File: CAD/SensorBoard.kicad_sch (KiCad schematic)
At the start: 37 parts, among them J1 USB C 2.0, SW1 BOOT_SW, U1 USBLC6-2SC6, U2 MIC5365-3.3YD5, U3 BME680, U4 TC1047xNB, U5 BMI323, X1 32MHz, X2 32kHz768

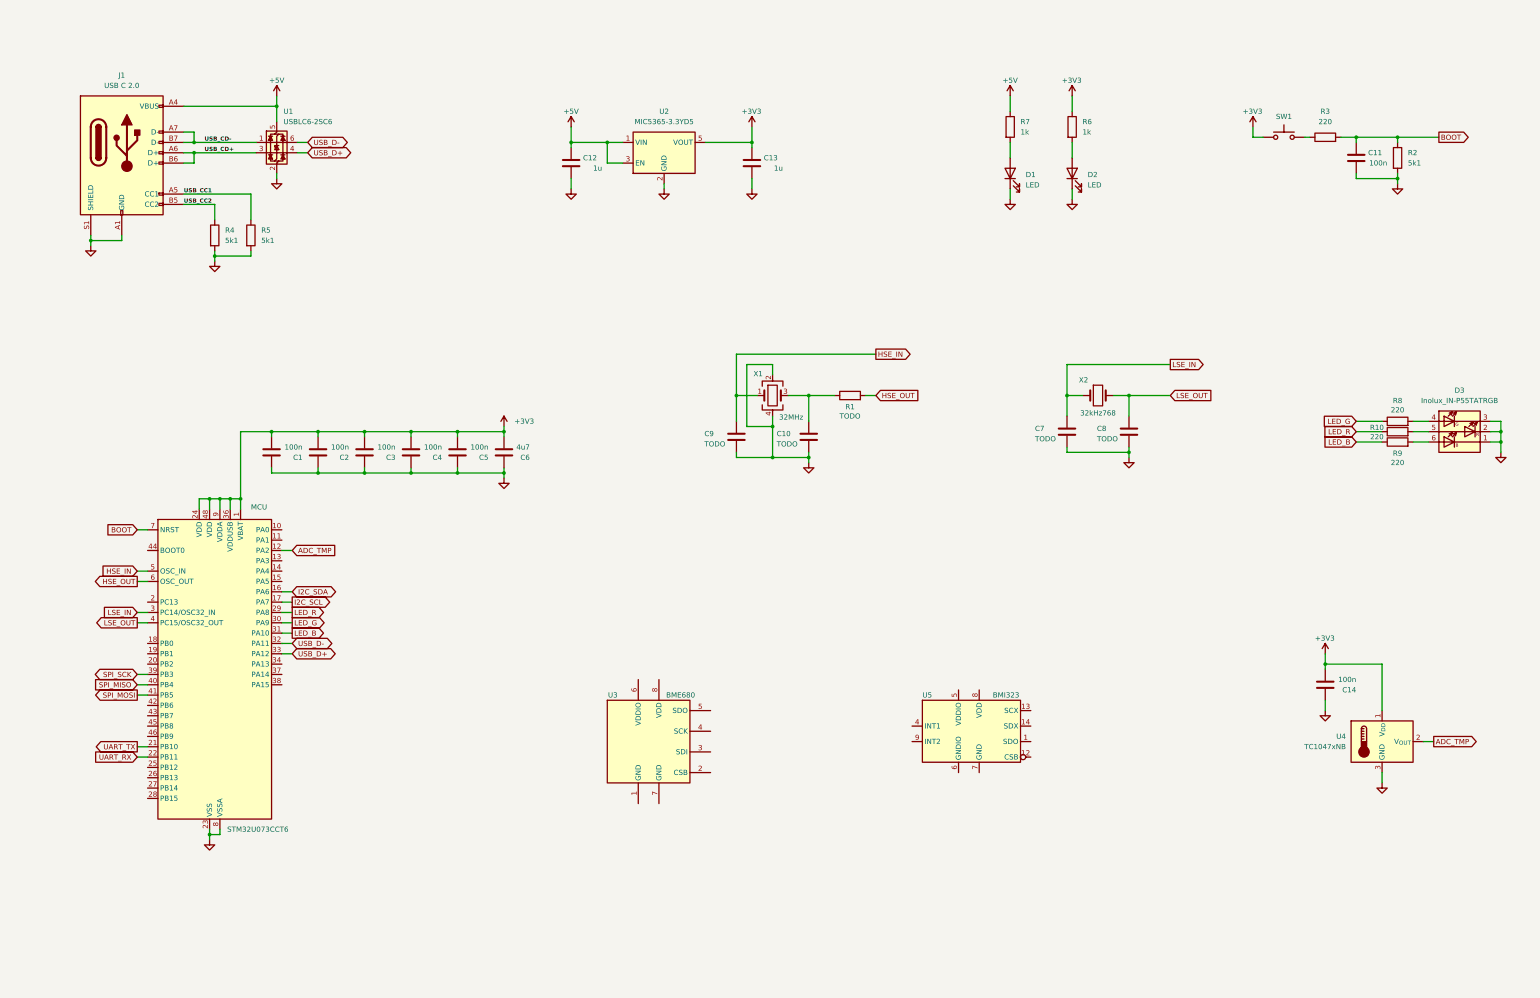
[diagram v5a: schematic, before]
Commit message: Update BME630 footprint
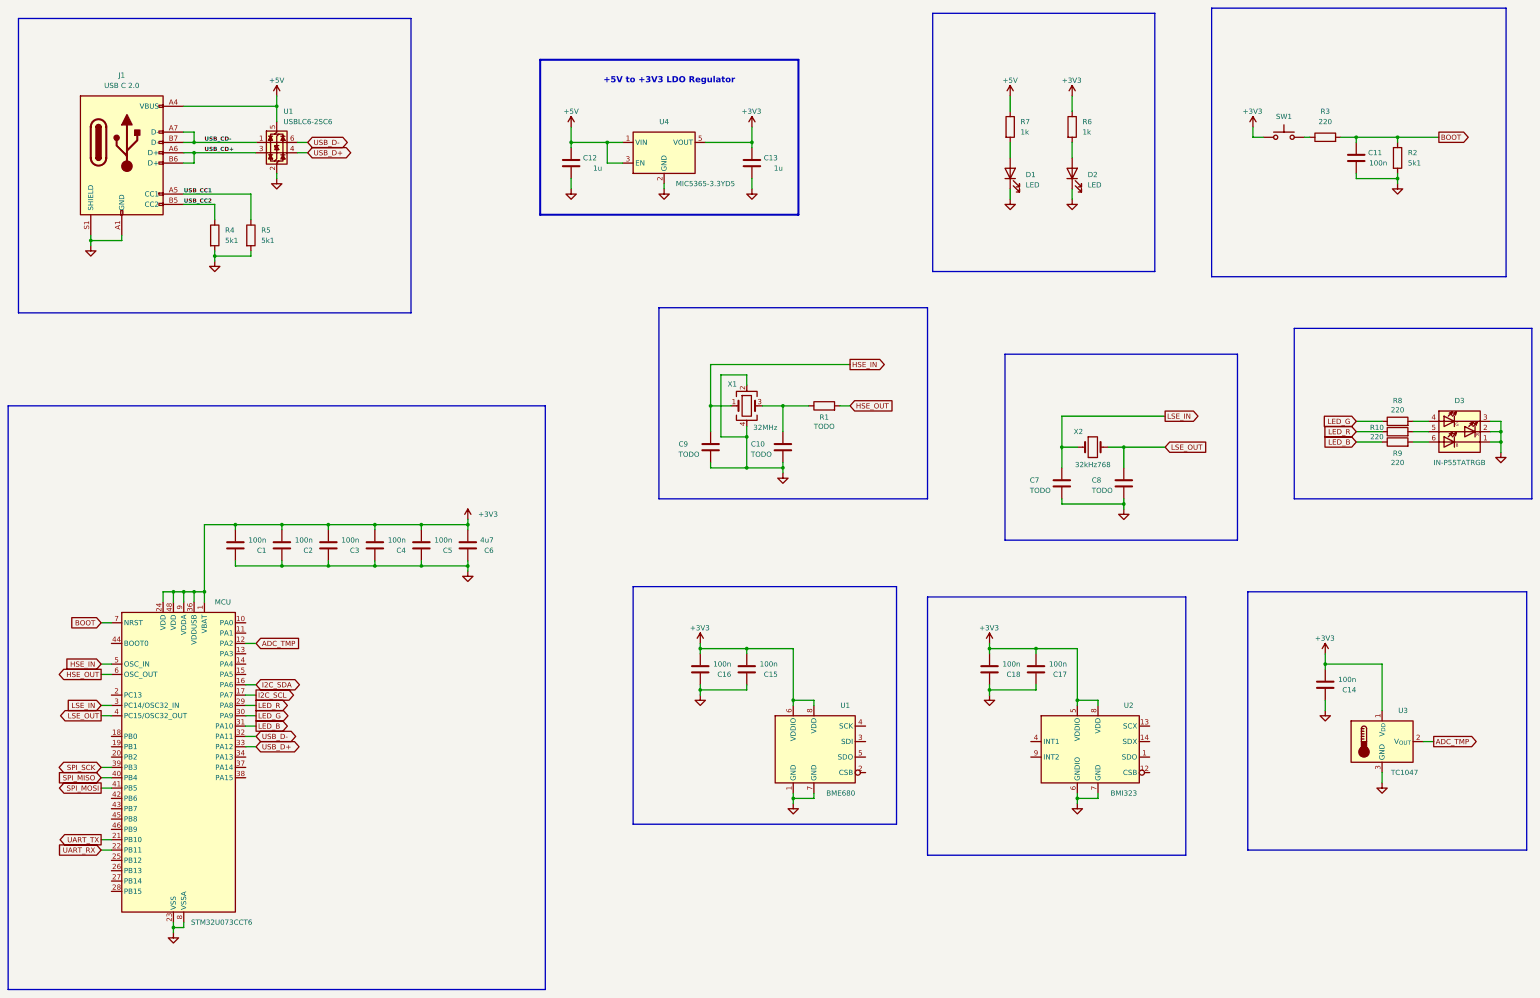
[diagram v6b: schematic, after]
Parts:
- added C15, C16, C17, C18: 100n, symbol Device:C
- D3: value Inolux_IN-P55TATRGB -> IN-P55TATRGB
- U1: renamed from U3; footprint Package_LGA:Bosch_LGA-8_3x3mm_P0.8mm_ClockwisePinNumbering -> SensorBoard:BME630; symbol Sensor:BME680 -> SensorBoard:BME630
- U3: renamed from U4; value TC1047xNB -> TC1047
- renumbered U5 to U2, U2 to U4
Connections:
- net +3V3: now also U1.6 (VDDIO), U1.8 (VDD), U2.5 (VDDIO), U2.8 (VDD), C15.2, C16.2, C17.2, C18.2
- net GND: now also U1.1 (GND), U1.7 (GND), U2.6 (GNDIO), U2.7 (GND), C15.1, C16.1, C17.1, C18.1
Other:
- note added: "+5V to +3V3 LDO Regulator"
- moved on the sheet: C1, C10, C2, C3, C4, C5, C6, C7, C8, C9, MCU, R1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

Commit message: Add I2C and SPI connections
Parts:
- added R11: 22, symbol Device:R
- added R12, R13: TODO, symbol Device:R
- renumbered MCU to U1, U1 to U2, U2 to U3, U3 to U4, U1 to U5, U4 to U6
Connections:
- net +3V3: now also U2.2 (CSB), R12.1, R13.1
- net GND: now also U2.5 (SDO)
- net I2C_SCL: now also U2.4 (SCK), R13.2
- net I2C_SDA: now also U2.3 (SDI), R12.2
- net SPI_MISO: now also U1.27 (PB14), U3.1 (SDO); no longer U1.40 (PB4)
- net SPI_MOSI: now also U1.28 (PB15), U3.14 (SDX); no longer U1.41 (PB5)
- net SPI_SCK: now also U3.13 (SCX), R11.1; no longer U1.39 (PB3)
- net SPI_NCS: now reaches U3.12 (CSB)
- net SPI_NCS: now also U1.25 (PB12)
- net IMU_INT1: now reaches U3.4 (INT1)
- net IMU_INT1: now also U1.19 (PB1)
- net IMU_INT2: now reaches U3.9 (INT2)
- net IMU_INT2: now also U1.20 (PB2)
- net SPI_SCK_R: now reaches U1.26 (PB13)
- net SPI_SCK_R: now also R11.2
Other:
- moved on the sheet: C1, C14, C15, C16, C17, C18, C2, C3, C4, C5, C6, U1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

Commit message: Add LEDs and buttons
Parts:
- added C19, C20, C21, C22: 100n, symbol Device:C
- added D4, D5, D6, D7: LED, symbol Device:LED
- added J2: ARM SWD TagConnect, Connector:Tag-Connect_TC2030-IDC-FP_2x03_P1.27mm_Vertical, symbol Connector:Conn_ARM_SWD_TagConnect_TC2030
- added R14, R15, R16, R17, R18, R20, R22, R24: 220, symbol Device:R
- added R19, R21, R23, R25: 5k1, symbol Device:R
- added SW2, SW3, SW4, SW5: BOOT_SW, symbol Switch:SW_Push
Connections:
- net +3V3: now also J2.1 (VCC), SW2.1, SW3.1, SW4.1, SW5.1
- net BOOT: now also U1.44 (BOOT0); no longer U1.7 (NRST)
- net GND: now also C19.1, C20.1, C21.1, C22.1, D4.1 (K), D5.1 (K), D6.1 (K), D7.1 (K), J2.5 (GND), R19.2, R21.2, R23.2, R25.2
- net LED_1: now reaches U1.10 (PA0)
- net LED_1: now also R14.1
- net LED_2: now reaches U1.11 (PA1)
- net LED_2: now also R15.1
- net LED_4: now reaches U1.13 (PA3)
- net LED_4: now also R17.1
- net DAC_OUT: now reaches U1.14 (PA4)
- net ADC_TEMP: now reaches U1.15 (PA5)
- net ADC_TEMP: now also U4.2 (V_{OUT})
- net SWD_DWDIO: now reaches U1.34 (PA13)
- net SWD_DWDIO: now also J2.2 (SWDIO)
- net SWD_SWCLK: now reaches U1.37 (PA14)
- net SWD_SWCLK: now also J2.4 (SWCLK)
- net SWD_SWO: now reaches U1.39 (PB3)
- net SWD_SWO: now also J2.6 (SWO)
- net BTN_1: now reaches U1.40 (PB4)
- net BTN_1: now also C19.2, R18.2, R19.1
- net BTN_2: now reaches U1.41 (PB5)
- net BTN_2: now also C20.2, R20.2, R21.1
- net BTN_3: now reaches U1.42 (PB6)
- net BTN_3: now also C21.2, R22.2, R23.1
- net BTN_4: now reaches U1.43 (PB7)
- net BTN_4: now also C22.2, R24.2, R25.1
- net ADC_TMP renamed LED_3
- net LED_3: now also R16.1; no longer U4.2 (V_{OUT})
- new net: D7.2 (A), R17.2
- new net: D5.2 (A), R15.2
- new net: R22.1, SW4.2
- new net: D6.2 (A), R16.2
- new net: D4.2 (A), R14.2
- new net: R24.1, SW5.2
- new net: R20.1, SW3.2
- new net: R18.1, SW2.2
- new net SWD_RST: J2.3 (~{RESET}), U1.7 (NRST)
- no-connect marks 0 -> 5
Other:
- moved on the sheet: C10, C11, C12, C13, C15, C16, C7, C8, C9, D1, D2, D3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
